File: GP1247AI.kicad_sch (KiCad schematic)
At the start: 17 parts, among them J1 Conn_02x05_Odd_Even, J2 Conn_02x05_Odd_Even

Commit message: Removed 8V boost converter
Now using an isolated 5V power supply module
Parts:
- removed TP1, TP2: TestPoint_Small, CustomFootprints:TestPoint_Keystone_5019_Miniature, symbol Connector:TestPoint_Small
- added U5: B0505S-2WR3, CustomFootprints:B0505S-2WR3, symbol CustomSymbols:B0505S-2WR3
- D1: footprint CustomFootprints:JSCJ 1SMB5913B -> Diode_SMD:D_SOD-123; LCSC PART # C5293672 -> C151564
- JP1: footprint Connector_PinHeader_2.54mm:PinHeader_1x02_P2.54mm_Vertical_SMD_Pin1Left -> Connector_PinHeader_2.54mm:PinHeader_1x02_P2.54mm_Vertical
- renumbered H3 to H2, H2 to H3
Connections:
- net +5V: now also J2.1 (Pin_1), J2.3 (Pin_3), U5.1 (+Vin)
- net F-: now also U5.4 (-Vout)
- net GND: now also U5.2 (-Vin)
- net +8V renamed F+
- net F+: now also U5.6 (+Vout); no longer J2.1 (Pin_1)
- no-connect marks 4 -> 1
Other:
- removed sheet 8V Boost
- note added: "C3031182 Dual rail 5V C5369434 Dual rail 12V"
- note removed: "1.32W Maximum dissipation use C286230 heat sink"
- note removed: "I considered using a flyback but that would be way more expensive"
- moved on the sheet: D1

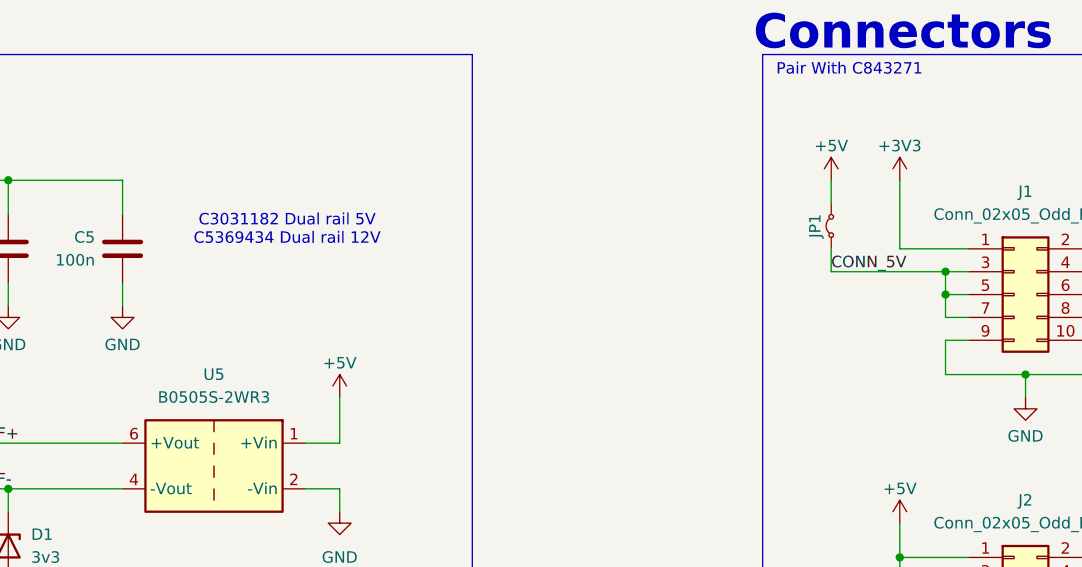
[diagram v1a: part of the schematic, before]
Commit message: Fixed boost2 feedback resistors
Old feedback resistor network made output voltage too high
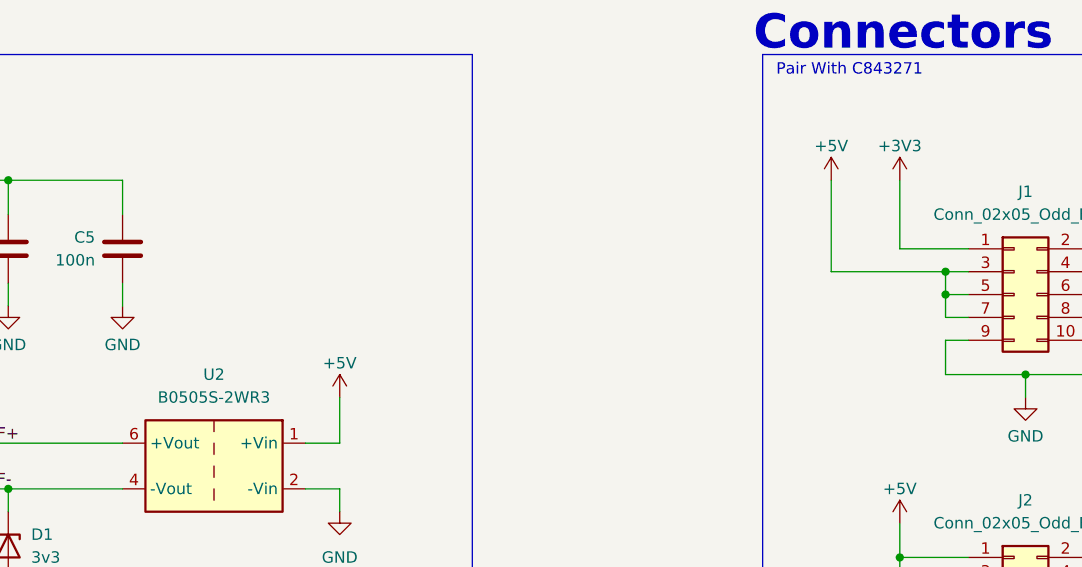
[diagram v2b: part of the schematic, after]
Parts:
- removed JP1: Jumper_2_Small_Bridged, Connector_PinHeader_2.54mm:PinHeader_1x02_P2.54mm_Vertical, symbol Jumper:Jumper_2_Small_Bridged
- J1, J2: footprint Connector_PinHeader_2.54mm:PinHeader_2x05_P2.54mm_Vertical_SMD -> Connector_PinHeader_2.54mm:PinHeader_2x05_P2.54mm_Vertical; LCSC PART # C32713285 -> C42431818
- renumbered U5 to U2
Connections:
- net CONN_5V is gone; now on net +5V: J1.3 (Pin_3), J1.5 (Pin_5), J1.7 (Pin_7)
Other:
- note removed: "C3031182 Dual rail 5V C5369434 Dual rail 12V"
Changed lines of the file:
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@@
 	(title_block
 		(title "GP1247AI Power Supply Board")
-		(date "2025-11-28")
-		(rev "2")
+		(date "2026-01-14")
 	)
 	(rectangle
@@
 		)
 	)
-	(text "C3031182 Dual rail 5V\nC5369434 Dual rail 12V"
-		(exclude_from_sim no)
-		(at 145.288 44.958 0)
-		(effects
-			(font
-				(size 1.27 1.27)
-			)
-		)
-	)
 	(text "Connectors"
 		(exclude_from_sim no)
@@
 	(wire
 		(pts
-			(xy 236.22 91.44) (xy 233.68 91.44)
+			(xy 205.74 39.37) (xy 205.74 49.53)
 		)
 		(stroke
@@
 	(wire
 		(pts
-			(xy 35.56 66.04) (xy 39.37 66.04)
+			(xy 236.22 91.44) (xy 233.68 91.44)
 		)
 		(stroke
@@
 	(wire
 		(pts
-			(xy 91.44 39.37) (xy 101.6 39.37)
+			(xy 35.56 66.04) (xy 39.37 66.04)
 		)
 		(stroke
@@
 	(wire
 		(pts
-			(xy 90.17 133.35) (xy 90.17 137.16)
+			(xy 91.44 39.37) (xy 101.6 39.37)
 		)
 		(stroke
@@
 	(wire
 		(pts
-			(xy 218.44 91.44) (xy 218.44 95.25)
+			(xy 90.17 133.35) (xy 90.17 137.16)
 		)
 		(stroke
@@
 	(wire
 		(pts
-			(xy 220.98 88.9) (xy 218.44 88.9)
+			(xy 218.44 91.44) (xy 218.44 95.25)
 		)
 		(stroke
@@
 	(wire
 		(pts
-			(xy 205.74 46.99) (xy 205.74 49.53)
+			(xy 220.98 88.9) (xy 218.44 88.9)
 		)
 		(stroke
@@
 	(wire
 		(pts
-			(xy 205.74 39.37) (xy 205.74 41.91)
-		)
-		(stroke
-			(width 0)
-			(type default)
-		)
-	)
-	(wire
-		(pts
 			(xy 218.44 49.53) (xy 220.98 49.53)
 		)
@@
 		)
 	)
-	(label "CONN_5V"
-		(at 205.74 49.53 0)
-		(effects
-			(font
-				(size 1.27 1.27)
-			)
-			(justify left bottom)
-		)
-	)
 	(label "TEST"
 		(at 81.28 57.15 90)
@@
 			)
 		)
-		(property "Footprint" "Connector_PinHeader_2.54mm:PinHeader_2x05_P2.54mm_Vertical_SMD"
+		(property "Footprint" "Connector_PinHeader_2.54mm:PinHeader_2x05_P2.54mm_Vertical"
 			(at 226.06 86.36 0)
 			(effects
@@
 			)
 		)
-		(property "Datasheet" "https://www.lcsc.com/datasheet/C32713285.pdf"
+		(property "Datasheet" "https://www.lcsc.com/datasheet/C42431818.pdf"
 			(at 226.06 86.36 0)
 			(effects
@@
 			)
 		)
-		(property "LCSC PART #" "C32713285"
+		(property "LCSC PART #" "C42431818"
 			(at 226.06 86.36 0)
 			(effects
@@
 	)
 	(symbol
-		(lib_id "Jumper:Jumper_2_Small_Bridged")
-		(at 205.74 44.45 90)
-		(unit 1)
-		(exclude_from_sim no)
-		(in_bom yes)
-		(on_board yes)
-		(dnp no)
-		(property "Reference" "JP1"
-			(at 203.962 44.45 0)
-			(effects
-				(font
-					(size 1.27 1.27)
-				)
-			)
-		)
-		(property "Value" "Jumper_2_Small_Bridged"
-			(at 203.2 44.45 0)
-			(effects
-				(font
-					(size 1.27 1.27)
-				)
-				(hide yes)
-			)
-		)
-		(property "Footprint" "Connector_PinHeader_2.54mm:PinHeader_1x02_P2.54mm_Vertical"
-			(at 205.74 44.45 0)
-			(effects
-				(font
-					(size 1.27 1.27)
-				)
-				(hide yes)
-			)
-		)
-		(property "Datasheet" "https://www.lcsc.com/datasheet/C41432920.pdf"
-			(at 205.74 44.45 0)
-			(effects
-				(font
-					(size 1.27 1.27)
-				)
-				(hide yes)
-			)
-		)
-		(property "Description" "Jumper, 2-pole, small symbol, bridged"
-			(at 205.74 44.45 0)
-			(effects
-				(font
-					(size 1.27 1.27)
-				)
-				(hide yes)
-			)
-		)
-		(property "LCSC PART #" "C41432920"
-			(at 205.74 44.45 0)
-			(effects
-				(font
-					(size 1.27 1.27)
-				)
-				(hide yes)
-			)
-		)
-		(pin "2"
-		)
-		(pin "1"
-		)
-		(instances
-			(project "GP1247AI"
-				(path "/152923e7-b4e9-428d-b807-06741b10ce95"
-					(reference "JP1")
-					(unit 1)
-				)
-			)
-		)
-	)
-	(symbol
 		(lib_id "Connector_Generic:Conn_02x05_Odd_Even")
 		(at 226.06 52.07 0)
@@
 			)
 		)
-		(property "Footprint" "Connector_PinHeader_2.54mm:PinHeader_2x05_P2.54mm_Vertical_SMD"
+		(property "Footprint" "Connector_PinHeader_2.54mm:PinHeader_2x05_P2.54mm_Vertical"
 			(at 226.06 52.07 0)
 			(effects
@@
 			)
 		)
-		(property "Datasheet" "https://www.lcsc.com/datasheet/C32713285.pdf"
+		(property "Datasheet" "https://www.lcsc.com/datasheet/C42431818.pdf"
 			(at 226.06 52.07 0)
 			(effects
@@
 			)
 		)
-		(property "LCSC PART #" "C32713285"
+		(property "LCSC PART #" "C42431818"
 			(at 226.06 52.07 0)
 			(effects
@@
 		(on_board yes)
 		(dnp no)
-		(property "Reference" "U5"
+		(property "Reference" "U2"
 			(at 137.16 60.96 0)
 			(effects
@@
 			(project ""
 				(path "/152923e7-b4e9-428d-b807-06741b10ce95"
-					(reference "U5")
+					(reference "U2")
 					(unit 1)
 				)
